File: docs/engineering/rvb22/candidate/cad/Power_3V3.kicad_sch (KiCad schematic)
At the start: 22 parts, among them U151 LM63615DQPWPRQ1

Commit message: fix(cca): reconcile controlled footprint variants and retain coupled thermal redlines
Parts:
- C154: footprint RevB:C_0603_1608Metric -> RevB:C_0603_1608Metric_RVB22_C154
- C206: footprint RevB:KEMET_T598_X_7343_Median -> RevB:KEMET_T598_X_7343_Median_RVB22_C206
- R155: footprint RevB:R_0603_1608Metric -> RevB:R_0603_1608Metric_RVB22_R155
- R156: footprint RevB:R_0603_1608Metric -> RevB:R_0603_1608Metric_RVB22_R156
- R157: footprint RevB:R_0603_1608Metric -> RevB:R_0603_1608Metric_RVB22_R157
- U151: footprint RevB:HTSSOP-16-1EP_4.4x5mm_P0.65mm_EP3.4x5mm_Mask2.46x2.31mm -> RevB:HTSSOP-16-1EP_4.4x5mm_P0.65mm_EP3.4x5mm_Mask2.46x2.31mm_RVB22_U151

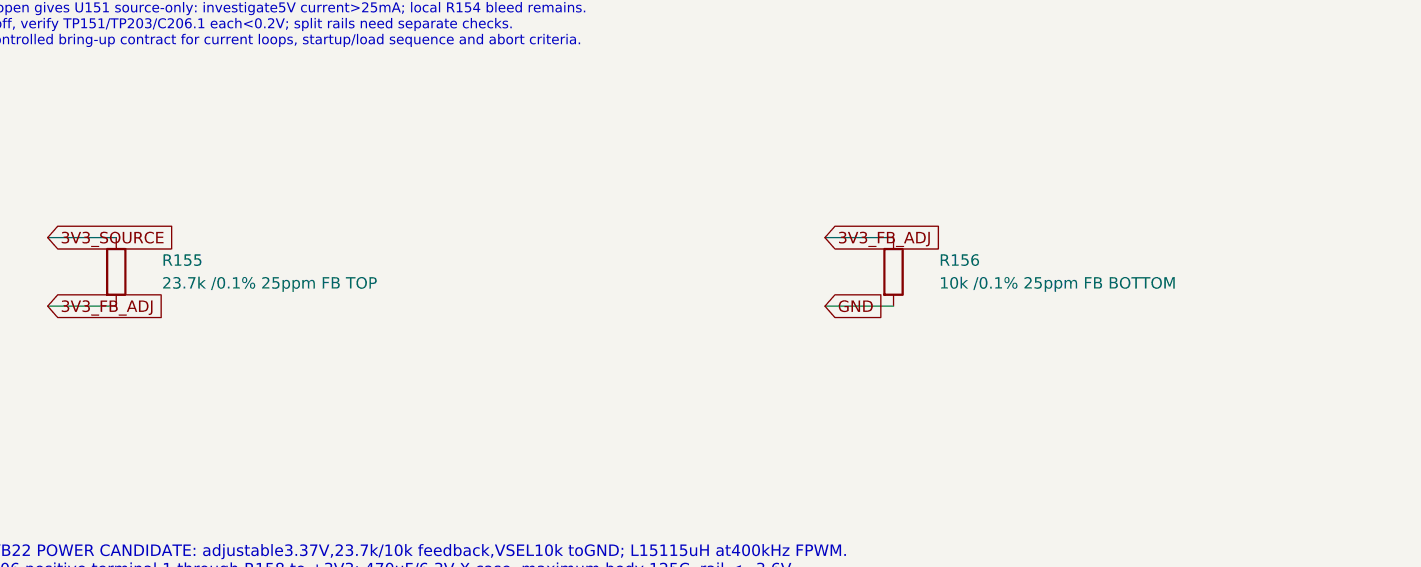
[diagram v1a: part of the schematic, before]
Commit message: RVB22 I19: tighten 3V3 feedback tolerance and thermal drift allocation
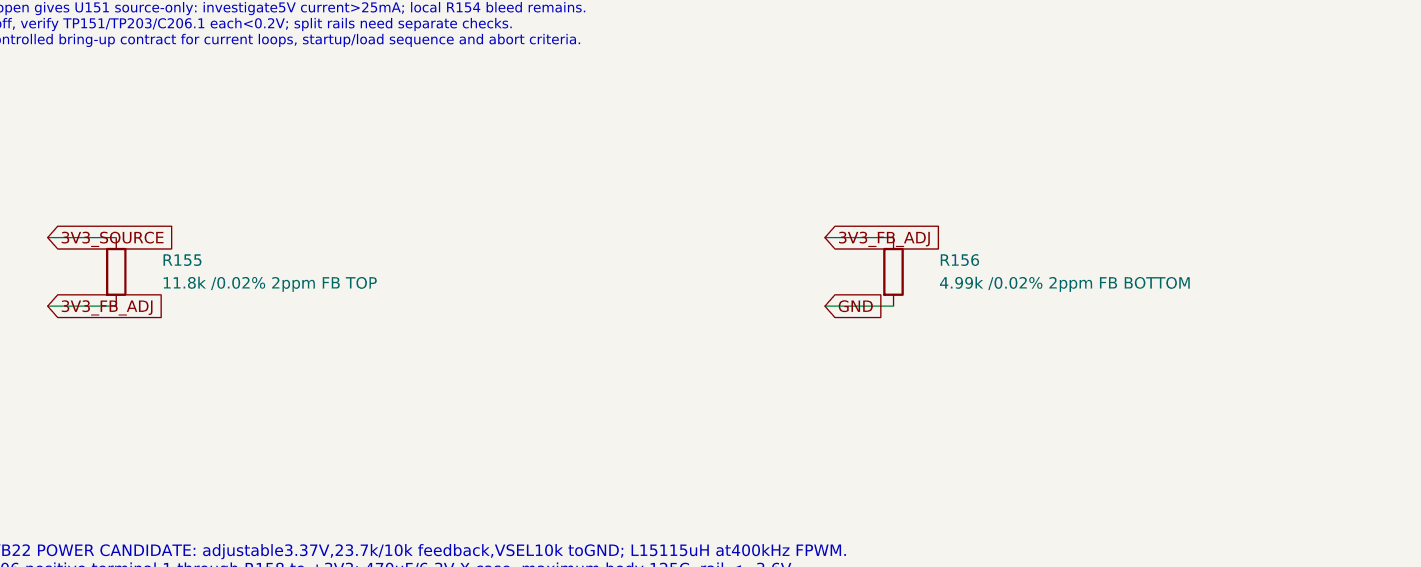
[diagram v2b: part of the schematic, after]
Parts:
- R155: value 23.7k /0.1% 25ppm FB TOP -> 11.8k /0.02% 2ppm FB TOP; MPN TNPW060323K7BEEA -> TNPU060311K8HWEA00
- R156: value 10k /0.1% 25ppm FB BOTTOM -> 4.99k /0.02% 2ppm FB BOTTOM; MPN TNPW060310K0BEEA -> TNPU06034K99HWEA00
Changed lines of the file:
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@@
 (global_label "3V3_FB_ADJ" (shape input) (at 114.3 290.83 0) (effects (font (size 1.27 1.27)) (justify left)) (property "Intersheetrefs" "${INTERSHEET_REFS}" (at 114.3 290.83 0) (effects (font (size 1.27 1.27)) hide)))
 (global_label "3V3_FB_ADJ" (shape input) (at 27.94 298.45 0) (effects (font (size 1.27 1.27)) (justify left)) (property "Intersheetrefs" "${INTERSHEET_REFS}" (at 27.94 298.45 0) (effects (font (size 1.27 1.27)) hide)))
-(symbol (lib_id "Device:R") (at 35.56 294.64 0) (unit 1) (in_bom yes) (on_board yes) (dnp no) (property "Reference" "R155" (at 40.64000000000004 293.37 0) (effects (font (size 1.27 1.27)) (justify left))) (property "Value" "23.7k /0.1% 25ppm FB TOP" (at 40.64000000000004 295.90999999999997 0) (effects (font (size 1.27 1.27)) (justify left))) (property "Footprint" "RevB:R_0603_1608Metric_RVB22_R155" (at 0 0 0) (effects (font (size 1.27 1.27)) (justify left) hide)) (property "Datasheet" "https://www.vishay.com/docs/28758/tnpw_e3.pdf" (at 0 0 0) (effects (font (size 1.27 1.27)) (justify left) hide)) (property "MPN" "TNPW060323K7BEEA" (at 0 0 0) (effects (font (size 1.27 1.27)) (justify left) hide)) (property "Qualification" "RVB22 reconstructed source candidate; native validation pending" (at 0 0 0) (effects (font (size 1.27 1.27)) (justify left) hide)) (pin "1") (pin "2") (instances (project "GR86_CCA_RevB" (path "/4108b523-946e-532e-b734-a3b8d9b0fa0b/4593baa2-c851-5487-8bf2-51d129d528a1" (reference "R155") (unit 1)))) (property "Manufacturer" "Vishay" (at 0 0 0) (effects (font (size 1.27 1.27)) (hide yes))) (property "LCSC" "" (at 0 0 0) (effects (font (size 1.27 1.27)) (hide yes))) (property "Assembly" "FACTORY" (at 0 0 0) (effects (font (size 1.27 1.27)) (hide yes))))
+(symbol (lib_id "Device:R") (at 35.56 294.64 0) (unit 1) (in_bom yes) (on_board yes) (dnp no) (property "Reference" "R155" (at 40.64000000000004 293.37 0) (effects (font (size 1.27 1.27)) (justify left))) (property "Value" "11.8k /0.02% 2ppm FB TOP" (at 40.64000000000004 295.90999999999997 0) (effects (font (size 1.27 1.27)) (justify left))) (property "Footprint" "RevB:R_0603_1608Metric_RVB22_R155" (at 0 0 0) (effects (font (size 1.27 1.27)) (justify left) hide)) (property "Datasheet" "https://www.vishay.com/docs/28779/tnpue3.pdf" (at 0 0 0) (effects (font (size 1.27 1.27)) (justify left) hide)) (property "MPN" "TNPU060311K8HWEA00" (at 0 0 0) (effects (font (size 1.27 1.27)) (justify left) hide)) (property "Qualification" "RVB22 reconstructed source candidate; native validation pending" (at 0 0 0) (effects (font (size 1.27 1.27)) (justify left) hide)) (pin "1") (pin "2") (instances (project "GR86_CCA_RevB" (path "/4108b523-946e-532e-b734-a3b8d9b0fa0b/4593baa2-c851-5487-8bf2-51d129d528a1" (reference "R155") (unit 1)))) (property "Manufacturer" "Vishay" (at 0 0 0) (effects (font (size 1.27 1.27)) (hide yes))) (property "LCSC" "" (at 0 0 0) (effects (font (size 1.27 1.27)) (hide yes))) (property "Assembly" "FACTORY" (at 0 0 0) (effects (font (size 1.27 1.27)) (hide yes))))
 (symbol (lib_id "Device:C") (at 381.0 294.64 0) (unit 1) (in_bom yes) (on_board yes) (dnp no) (property "Reference" "C206" (at 386.08 293.37 0) (effects (font (size 1.27 1.27)) (justify left))) (property "Value" "470u /6.3V POLYMER" (at 386.08 295.90999999999997 0) (effects (font (size 1.27 1.27)) (justify left))) (property "Footprint" "RevB:KEMET_T598_X_7343_Median_RVB22_C206" (at 0 0 0) (effects (font (size 1.27 1.27)) (justify left) hide)) (property "Datasheet" "https://content.kemet.com/datasheets/KEM_T2073_T59X.pdf" (at 0 0 0) (effects (font (size 1.27 1.27)) (justify left) hide)) (property "MPN" "T598X477M006ATE025" (at 0 0 0) (effects (font (size 1.27 1.27)) (justify left) hide)) (property "Qualification" "RVB22 reconstructed source candidate; native validation pending" (at 0 0 0) (effects (font (size 1.27 1.27)) (justify left) hide)) (pin "1") (pin "2") (instances (project "GR86_CCA_RevB" (path "/4108b523-946e-532e-b734-a3b8d9b0fa0b/4593baa2-c851-5487-8bf2-51d129d528a1" (reference "C206") (unit 1)))) (property "Manufacturer" "KEMET" (at 0 0 0) (effects (font (size 1.27 1.27)) (hide yes))) (property "LCSC" "" (at 0 0 0) (effects (font (size 1.27 1.27)) (hide yes))) (property "Assembly" "FACTORY" (at 0 0 0) (effects (font (size 1.27 1.27)) (hide yes))))
 (symbol (lib_id "Device:R") (at 294.64 294.64 0) (unit 1) (in_bom yes) (on_board yes) (dnp no) (property "Reference" "R158" (at 299.72 293.37 0) (effects (font (size 1.27 1.27)) (justify left))) (property "Value" "82m /1% BULK DAMPING" (at 299.72 295.90999999999997 0) (effects (font (size 1.27 1.27)) (justify left))) (property "Footprint" "RevB:WSLP0603_MANUFACTURER" (at 0 0 0) (effects (font (size 1.27 1.27)) (justify left) hide)) (property "Datasheet" "https://www.vishay.com/docs/30122/wslp.pdf" (at 0 0 0) (effects (font (size 1.27 1.27)) (justify left) hide)) (property "MPN" "WSLP0603R0820FEA" (at 0 0 0) (effects (font (size 1.27 1.27)) (justify left) hide)) (property "Qualification" "RVB22 reconstructed source candidate; native validation pending" (at 0 0 0) (effects (font (size 1.27 1.27)) (justify left) hide)) (pin "1") (pin "2") (instances (project "GR86_CCA_RevB" (path "/4108b523-946e-532e-b734-a3b8d9b0fa0b/4593baa2-c851-5487-8bf2-51d129d528a1" (reference "R158") (unit 1)))) (property "Manufacturer" "Vishay" (at 0 0 0) (effects (font (size 1.27 1.27)) (hide yes))) (property "LCSC" "" (at 0 0 0) (effects (font (size 1.27 1.27)) (hide yes))) (property "Assembly" "FACTORY" (at 0 0 0) (effects (font (size 1.27 1.27)) (hide yes))))
 (symbol (lib_id "Device:R") (at 208.28 294.64 0) (unit 1) (in_bom yes) (on_board yes) (dnp no) (property "Reference" "R157" (at 213.36000000000004 293.37 0) (effects (font (size 1.27 1.27)) (justify left))) (property "Value" "10k /1% VSEL ADJUST" (at 213.36000000000004 295.90999999999997 0) (effects (font (size 1.27 1.27)) (justify left))) (property "Footprint" "RevB:R_0603_1608Metric_RVB22_R157" (at 0 0 0) (effects (font (size 1.27 1.27)) (justify left) hide)) (property "Datasheet" "https://www.vishay.com/docs/20035/dcrcwe3.pdf" (at 0 0 0) (effects (font (size 1.27 1.27)) (justify left) hide)) (property "MPN" "CRCW060310K0FKEA" (at 0 0 0) (effects (font (size 1.27 1.27)) (justify left) hide)) (property "Qualification" "RVB22 reconstructed source candidate; native validation pending" (at 0 0 0) (effects (font (size 1.27 1.27)) (justify left) hide)) (pin "1") (pin "2") (instances (project "GR86_CCA_RevB" (path "/4108b523-946e-532e-b734-a3b8d9b0fa0b/4593baa2-c851-5487-8bf2-51d129d528a1" (reference "R157") (unit 1)))) (property "Manufacturer" "Vishay" (at 0 0 0) (effects (font (size 1.27 1.27)) (hide yes))) (property "LCSC" "" (at 0 0 0) (effects (font (size 1.27 1.27)) (hide yes))) (property "Assembly" "FACTORY" (at 0 0 0) (effects (font (size 1.27 1.27)) (hide yes))))
-(symbol (lib_id "Device:R") (at 121.92 294.64 0) (unit 1) (in_bom yes) (on_board yes) (dnp no) (property "Reference" "R156" (at 127.00000000000006 293.37 0) (effects (font (size 1.27 1.27)) (justify left))) (property "Value" "10k /0.1% 25ppm FB BOTTOM" (at 127.00000000000006 295.90999999999997 0) (effects (font (size 1.27 1.27)) (justify left))) (property "Footprint" "RevB:R_0603_1608Metric_RVB22_R156" (at 0 0 0) (effects (font (size 1.27 1.27)) (justify left) hide)) (property "Datasheet" "https://www.vishay.com/docs/28758/tnpw_e3.pdf" (at 0 0 0) (effects (font (size 1.27 1.27)) (justify left) hide)) (property "MPN" "TNPW060310K0BEEA" (at 0 0 0) (effects (font (size 1.27 1.27)) (justify left) hide)) (property "Qualification" "RVB22 reconstructed source candidate; native validation pending" (at 0 0 0) (effects (font (size 1.27 1.27)) (justify left) hide)) (pin "1") (pin "2") (instances (project "GR86_CCA_RevB" (path "/4108b523-946e-532e-b734-a3b8d9b0fa0b/4593baa2-c851-5487-8bf2-51d129d528a1" (reference "R156") (unit 1)))) (property "Manufacturer" "Vishay" (at 0 0 0) (effects (font (size 1.27 1.27)) (hide yes))) (property "LCSC" "" (at 0 0 0) (effects (font (size 1.27 1.27)) (hide yes))) (property "Assembly" "FACTORY" (at 0 0 0) (effects (font (size 1.27 1.27)) (hide yes))))
+(symbol (lib_id "Device:R") (at 121.92 294.64 0) (unit 1) (in_bom yes) (on_board yes) (dnp no) (property "Reference" "R156" (at 127.00000000000006 293.37 0) (effects (font (size 1.27 1.27)) (justify left))) (property "Value" "4.99k /0.02% 2ppm FB BOTTOM" (at 127.00000000000006 295.90999999999997 0) (effects (font (size 1.27 1.27)) (justify left))) (property "Footprint" "RevB:R_0603_1608Metric_RVB22_R156" (at 0 0 0) (effects (font (size 1.27 1.27)) (justify left) hide)) (property "Datasheet" "https://www.vishay.com/docs/28779/tnpue3.pdf" (at 0 0 0) (effects (font (size 1.27 1.27)) (justify left) hide)) (property "MPN" "TNPU06034K99HWEA00" (at 0 0 0) (effects (font (size 1.27 1.27)) (justify left) hide)) (property "Qualification" "RVB22 reconstructed source candidate; native validation pending" (at 0 0 0) (effects (font (size 1.27 1.27)) (justify left) hide)) (pin "1") (pin "2") (instances (project "GR86_CCA_RevB" (path "/4108b523-946e-532e-b734-a3b8d9b0fa0b/4593baa2-c851-5487-8bf2-51d129d528a1" (reference "R156") (unit 1)))) (property "Manufacturer" "Vishay" (at 0 0 0) (effects (font (size 1.27 1.27)) (hide yes))) (property "LCSC" "" (at 0 0 0) (effects (font (size 1.27 1.27)) (hide yes))) (property "Assembly" "FACTORY" (at 0 0 0) (effects (font (size 1.27 1.27)) (hide yes))))
 (text "+ pin 1" (at 378.46 293.37 0) (effects (font (size 1.27 1.27)) (justify right)))
 (text "RVB22 POWER CANDIDATE: adjustable3.37V,23.7k/10k feedback,VSEL10k toGND; L15115uH at400kHz FPWM.\nC206 positive terminal 1 through R158 to +3V3; 470uF/6.3V X case, maximum body 125C, rail <=3.6V.\nR15882mOhm: finite actual tapped/parallel distribution verification passed; model conditions apply.\nNative ERC/refill/DRC not run; numerical model conditions are controlled separately." (at 20.32 325.12 0) (effects (font (size 1.27 1.27)) (justify left top)))

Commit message: RVB22 I20: reconcile current power notes and engineering effectivity
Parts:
- C206, R155, R156, R157, R158: Qualification RVB22 reconstructed source candidate; native validation pen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 -> RVB22 engineering candidate; see current native evidence an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
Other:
- note added: "RVB22 POWER CANDIDATE: adjustable3.36473V,11.8k/4.99k feedback,VSEL10k toGND; L15115uH at400kHz FPWM. C206 positive terminal 1 through R158 to +3V3; 470uF/6.3V X case, maximum body 125C, rail <=3.6V. R15882mOhm: finite actual tapped/parallel distribution verification passed; model conditions apply. I19 native ERC/refill/DRC and target build passed; current I20 report and model conditions control."
- note added: "RVB22 — ADJUSTABLE3.36473V MAIN /0.75A ALLOCATION /1.5A CONVERTER R15710k selects adjustable VSEL; R15511.8k/R1564.99k (TNPU0.02%,2ppm/K) set FB. RT=VCC, SYNC/MODE=VCC. L15115uH XGL5030-153MEC;400kHz FPWM. Source bound3.306564–3.423112V including stated drift before distribution drop. FB senses source capacitor bank; compare source/local rail and EN under load."
- note removed: "RVB22 POWER CANDIDATE: adjustable3.37V,23.7k/10k feedback,VSEL10k toGND; L15115uH at400kHz FPWM. C206 positive terminal 1 through R158 to +3V3; 470uF/6.3V X case, maximum body 125C, rail <=3.6V. R15882mOhm: finite actual tapped/parallel distribution verification passed; model conditions apply. Native ERC/refill/DRC not run; numerical model conditions are controlled separately."
- note removed: "RVB22 — ADJUSTABLE3.37V MAIN /0.75A ALLOCATION /1.5A CONVERTER R15710k selects adjustable VSEL; R15523.7k/R15610k set FB. RT=VCC, SYNC/MODE=VCC. L15115uH XGL5030-153MEC;400kHz FPWM. Source tolerance3.297890–3.442858V before distribution drop. FB senses source capacitor bank; compare source/local rail and EN under load."
